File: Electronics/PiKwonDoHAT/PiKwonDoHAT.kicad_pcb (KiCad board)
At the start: 2 copper layers, 55 x 63 mm, 42 parts, among them CN1 Conn_02x20_Odd_Even, CN2 Judge1, CN3 Judge2, CN4 Judge3, CN5 Controller, U1 74LV1T34, U2 74LV1T34, U3 74LV1T34, U4 74LV1T34

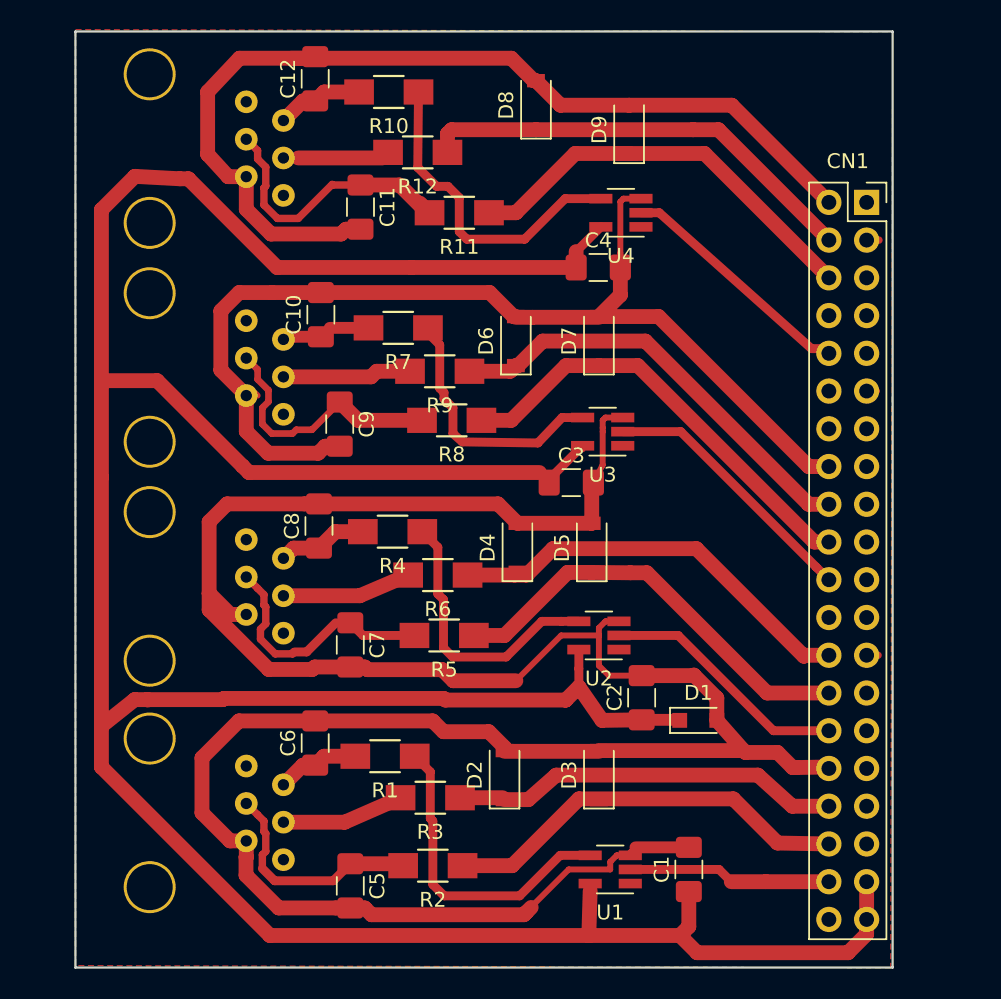
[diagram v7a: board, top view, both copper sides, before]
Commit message: Updated trace routing and RJ12 footprint.
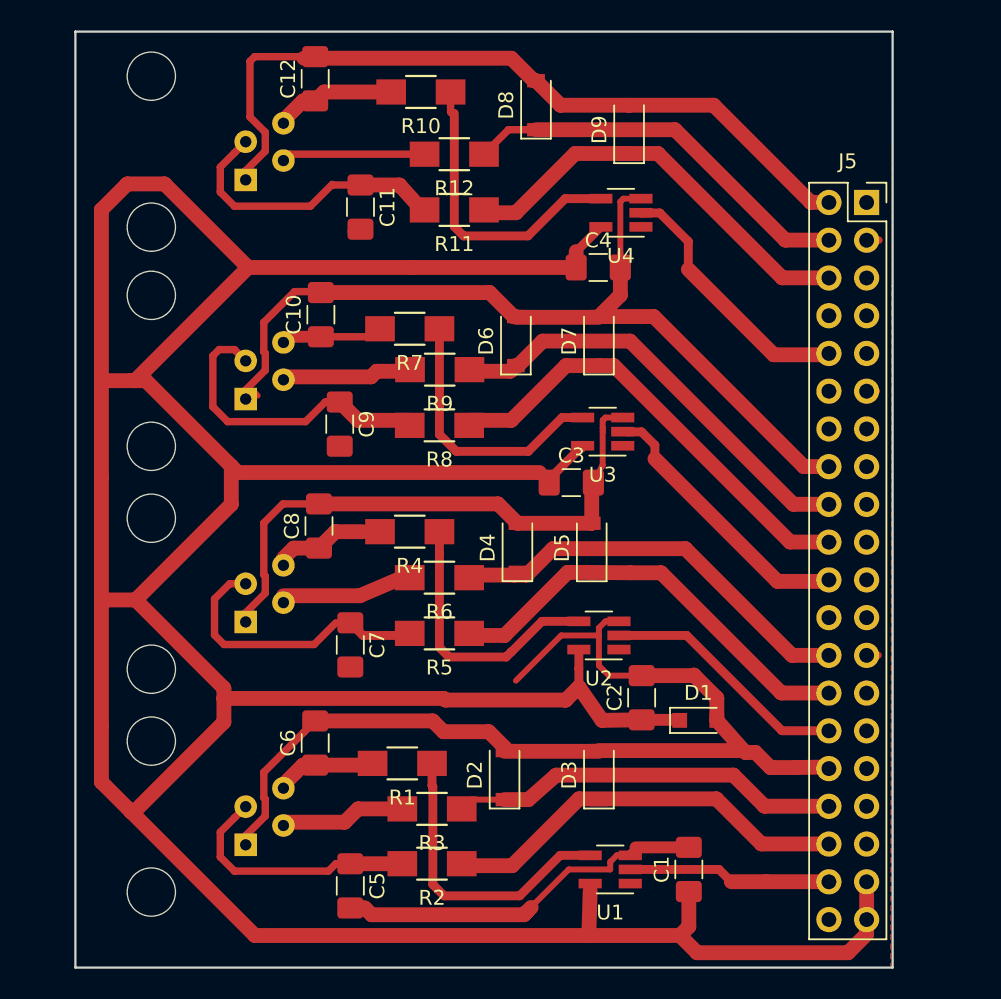
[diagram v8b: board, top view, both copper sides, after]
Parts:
- removed CN1: Conn_02x20_Odd_Even, Connector_PinSocket_2.54mm:PinSocket_2x20_P2.54mm_Vertical
- removed CN2: Judge1, PiKwonDo:TH-RJ12
- removed CN3: Judge2, PiKwonDo:TH-RJ12
- removed CN4: Judge3, PiKwonDo:TH-RJ12
- removed CN5: Controller, PiKwonDo:TH-RJ12
- added J1: RJ10, Local_lib:RJ14, B.Cu at (84.0, 126.0)
- added J2: RJ10, Local_lib:RJ14, B.Cu at (84.0, 111.0)
- added J3: RJ10, Local_lib:RJ14, B.Cu at (84.0, 96.0)
- added J4: RJ10, Local_lib:RJ14, B.Cu at (84.0, 81.2)
- added J5: Conn_02x20_Odd_Even, Connector_PinSocket_2.54mm:PinSocket_2x20_P2.54mm_Vertical, F.Cu at (123.2, 81.5)
- moved R12 2.46 mm to (95.5, 78.2)
- moved R10 2.16 mm to (93.2, 74.1)
- moved R1 1.26 mm to (92.0, 119.2)
- moved R4 1.16 mm to (92.5, 103.7)
- moved R8 0.89 mm to (94.5, 96.5)
- moved R7 0.78 mm to (92.5, 90.0)
- moved R3 0.76 mm to (94.0, 122.3)
- moved R11 0.39 mm to (95.5, 82.0)
- moved R5 0.35 mm to (94.5, 110.5)
- moved R6 0.20 mm to (94.5, 106.8)
- moved R2 0.15 mm to (94.0, 126.0)
- moved R9 0.11 mm to (94.5, 92.8)
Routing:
- net GND: track 318.0 -> 248.1 mm
- net +5V: track 223.4 -> 258.9 mm
- net Net-(C9-Pad1): track 17.6 -> 20.9 mm
- net /C_DATA: track 30.1 -> 27.0 mm
- net Net-(C7-Pad1): track 17.0 -> 19.6 mm
- net Net-(C12-Pad1): track 5.89 -> 8.05 mm
- net Net-(J4-Pad2): track 7.53 -> 9.68 mm
- net Net-(C5-Pad1): track 15.4 -> 17.1 mm
- net /C_CLK: track 16.3 -> 17.8 mm
- net Net-(R10-Pad1): track 21.9 -> 20.4 mm
- net Net-(J5-Pad25): track 0.00 -> 1.32 mm
- net Net-(CN1-Pad25): track 1.32 -> 0.00 mm
- net Net-(R1-Pad1): track 21.2 -> 20.2 mm
- net Net-(C11-Pad1): track 19.2 -> 20.0 mm
- net Net-(J5-Pad3): track 0.00 -> 0.83 mm
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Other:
- net class Default: clearance 0.3 -> 0.31; trace_width 0.4 -> 0.5
- rule trace_clearance: 0.3 -> 0.31
